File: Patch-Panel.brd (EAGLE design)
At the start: 84.9 x 142.3 mm, 66 parts, among them J1 APPPP45_PCB_VERT, J10 APPPP45_PCB_VERT, J11 APPPP45_PCB_VERT, J12 APPPP45_PCB_VERT, J13 APPPP45_PCB_VERT, J14 APPPP45_PCB_VERT, J15 APPPP45_PCB_VERT, J16 APPPP45_PCB_VERT, J17 APPPP45_PCB_VERT, J18 APPPP45_PCB_VERT, J19 APPPP45_PCB_VERT, J2 APPPP45_PCB_VERT, J20 APPPP45_PCB_VERT, J21 APPPP45_PCB_VERT, J22 APPPP45_PCB_VERT, J23 APPPP45_PCB_VERT, J24 APPPP45_PCB_VERT, J25 APPPP45_PCB_VERT, J26 APPPP45_PCB_VERT, J27 APPPP45_PCB_VERT, J28 APPPP45_PCB_VERT, J29 APPPP45_PCB_VERT, J3 APPPP45_PCB_VERT, J30 APPPP45_PCB_VERT, J31 APPPP45_PCB_VERT, J32 APPPP45_PCB_VERT, J33 APPPP45_PCB_VERT, J34 APPPP45_PCB_VERT, J35 APPPP45_PCB_VERT, J36 APPPP45_PCB_VERT, J37 APPPP45_PCB_VERT, J38 APPPP45_PCB_VERT, J39 APPPP45_PCB_VERT, J4 APPPP45_PCB_VERT, J40 APPPP45_PCB_VERT, J41 APPPP45_PCB_VERT, J42 APPPP45_PCB_VERT, J43 APPPP45_PCB_VERT, J44 APPPP45_PCB_VERT, J45 APPPP45_PCB_VERT, J46 APPPP45_PCB_VERT, J47 APPPP45_PCB_VERT, J48 APPPP45_PCB_VERT, J49 APPPP45_PCB_VERT, J5 APPPP45_PCB_VERT, J50 APPPP45_PCB_VERT, J51 APPPP45_PCB_VERT, J52 APPPP45_PCB_VERT, J53 APPPP45_PCB_VERT, J54 APPPP45_PCB_VERT, J55 APPPP45_PCB_VERT, J56 APPPP45_PCB_VERT, J57 APPPP45_PCB_VERT, J58 APPPP45_PCB_VERT, J6 APPPP45_PCB_VERT, J7 APPPP45_PCB_VERT, J8 APPPP45_PCB_VERT, J9 APPPP45_PCB_VERT

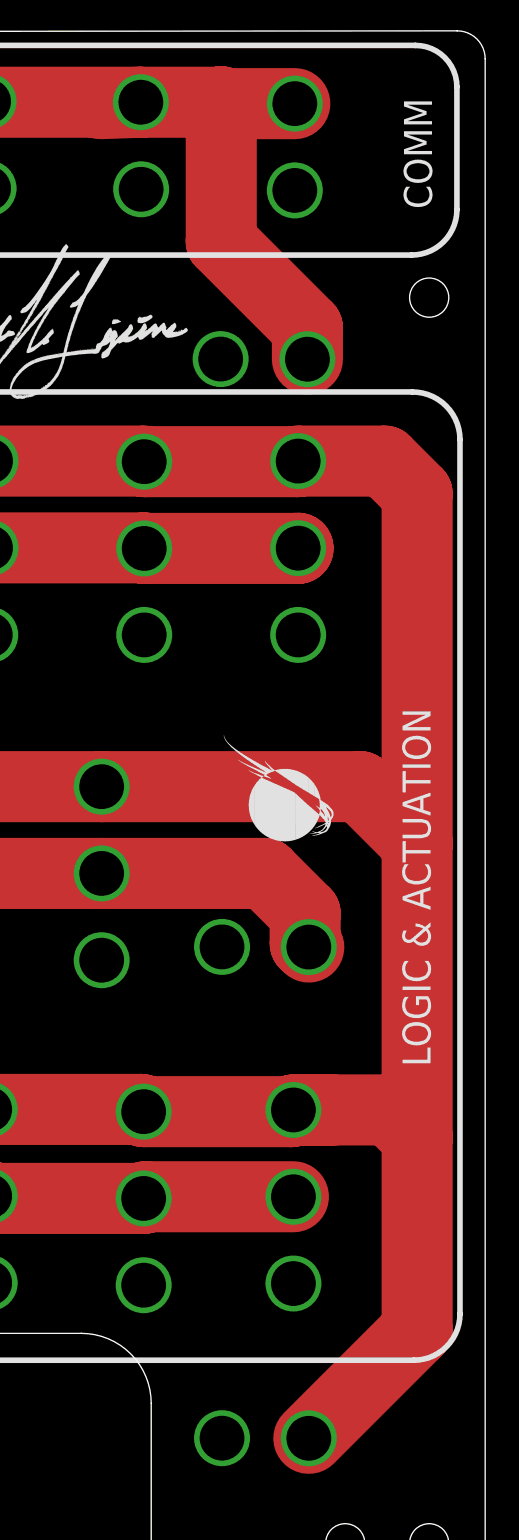
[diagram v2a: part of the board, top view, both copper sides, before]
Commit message: Adjusted bottom anderson positions
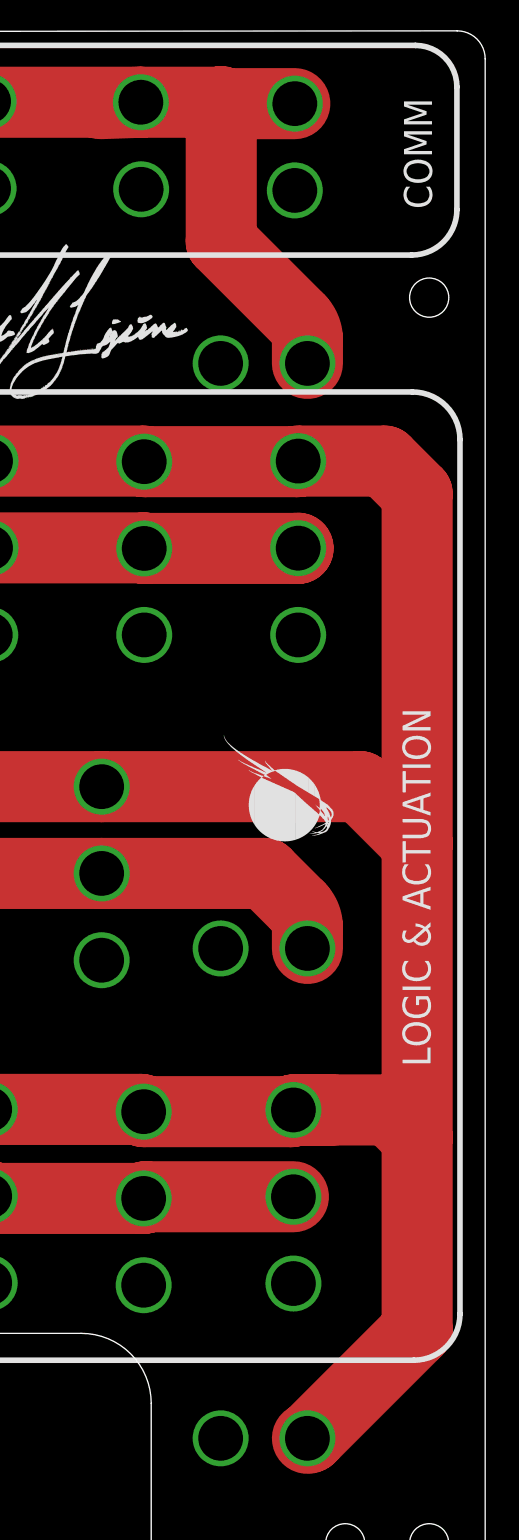
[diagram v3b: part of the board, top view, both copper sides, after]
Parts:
- moved J4 0.39 mm to (57.0, 115.3)
- moved J5 0.38 mm to (64.8, 115.3)
- moved J6 0.19 mm to (57.0, 62.2)
- moved J3 0.18 mm to (64.8, 62.2)
- moved J2 0.13 mm to (57.0, 17.8)
- moved J1 0.13 mm to (64.8, 17.8)
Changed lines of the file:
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@@
 <setting verticaltext="up"/>
 </settings>
-<grid distance="10" unitdist="mil" unit="mil" style="lines" multiple="1" display="yes" altdistance="5" altunitdist="mil" altunit="mil"/>
+<grid distance="1" unitdist="mil" unit="mil" style="lines" multiple="1" display="yes" altdistance="5" altunitdist="mil" altunit="mil"/>
 <layers>
 <layer number="1" name="Top" color="4" fill="1" visible="yes" active="yes"/>
@@
 <dimension x1="35.56" y1="24.13" x2="16.7894" y2="0" x3="-8.763" y3="12.065" textsize="1.778" layer="47" dtype="vertical" unit="mil"/>
 <wire x1="32.258" y1="120.142" x2="32.258" y2="112.014" width="0.254" layer="21"/>
+<dimension x1="82.3722" y1="0" x2="72.898" y2="9.906" x3="93.218" y3="4.953" textsize="1.4224" layer="21" dtype="vertical" unit="mil"/>
+<dimension x1="84.9122" y1="2.54" x2="72.7202" y2="10.9474" x3="78.8162" y3="-9.525" textsize="1.4224" layer="21" dtype="horizontal" unit="mil"/>
+<dimension x1="84.9122" y1="2.54" x2="72.7202" y2="10.414" x3="78.8162" y3="63.5254" textsize="1.4224" layer="21" dtype="horizontal" unit="mil"/>
+<dimension x1="82.3722" y1="0" x2="72.7202" y2="107.442" x3="112.903" y3="53.721" textsize="1.4224" layer="47" dtype="vertical" unit="mil"/>
+<dimension x1="82.3722" y1="0" x2="72.7202" y2="54.356" x3="98.1202" y3="27.178" textsize="1.4224" layer="47" dtype="vertical" unit="mil"/>
 </plain>
 <attributes>
@@
 </autorouter>
 <elements>
-<element name="J1" library="MRDT-Connectors" package="APP45_PCB_VERT" value="APPPP45_PCB_VERT" x="64.9732" y="17.78" rot="MR180">
-<attribute name="COLOR1" value="" x="64.9732" y="17.78" size="1.778" layer="28" rot="MR180" display="off"/>
+<element name="J1" library="MRDT-Connectors" package="APP45_PCB_VERT" value="APPPP45_PCB_VERT" x="64.8462" y="17.78" rot="MR180">
+<attribute name="COLOR1" value="" x="64.8462" y="17.78" size="1.778" layer="28" rot="MR180" display="off"/>
 </element>
 <element name="J10" library="MRDT-Connectors" package="APP45_PCB_VERT" value="APPPP45_PCB_VERT" x="50.7492" y="32.4358" rot="R270">
@@
 <attribute name="COLOR1" value="" x="34.2392" y="61.8744" size="1.778" layer="27" rot="R270" display="off"/>
 </element>
-<element name="J2" library="MRDT-Connectors" package="APP45_PCB_VERT" value="APPPP45_PCB_VERT" x="57.0992" y="17.7927" rot="MR180">
-<attribute name="COLOR1" value="" x="57.0992" y="17.7927" size="1.778" layer="28" rot="MR180" display="off"/>
+<element name="J2" library="MRDT-Connectors" package="APP45_PCB_VERT" value="APPPP45_PCB_VERT" x="56.9722" y="17.78" rot="MR180">
+<attribute name="COLOR1" value="" x="56.9722" y="17.78" size="1.778" layer="28" rot="MR180" display="off"/>
 </element>
 <element name="J20" library="MRDT-Connectors" package="APP45_PCB_VERT" value="APPPP45_PCB_VERT" x="34.2392" y="69.7484" rot="R270">
@@
 <attribute name="COLOR1" value="" x="46.9392" y="61.9252" size="1.778" layer="27" rot="R270" display="off"/>
 </element>
-<element name="J3" library="MRDT-Connectors" package="APP45_PCB_VERT" value="APPPP45_PCB_VERT" x="64.9732" y="62.357" rot="MR180">
-<attribute name="COLOR1" value="" x="64.9732" y="62.357" size="1.778" layer="28" rot="MR180" display="off"/>
+<element name="J3" library="MRDT-Connectors" package="APP45_PCB_VERT" value="APPPP45_PCB_VERT" x="64.8462" y="62.23" rot="MR180">
+<attribute name="COLOR1" value="" x="64.8462" y="62.23" size="1.778" layer="28" rot="MR180" display="off"/>
 </element>
 <element name="J30" library="MRDT-Connectors" package="APP45_PCB_VERT" value="APPPP45_PCB_VERT" x="64.4652" y="139.6492" rot="R270">
@@
 <attribute name="COLOR1" value="" x="22.7076" y="131.9784" size="1.778" layer="27" rot="R270" display="off"/>
 </element>
-<element name="J4" library="MRDT-Connectors" package="APP45_PCB_VERT" value="APPPP45_PCB_VERT" x="56.9722" y="115.7097" rot="MR180">
-<attribute name="COLOR1" value="" x="56.9722" y="115.7097" size="1.778" layer="28" rot="MR180" display="off"/>
-</element>
-<element name="J5" library="MRDT-Connectors" package="APP45_PCB_VERT" value="APPPP45_PCB_VERT" x="64.8462" y="115.697" rot="MR180">
-<attribute name="COLOR1" value="" x="64.8462" y="115.697" size="1.778" layer="28" rot="MR180" display="off"/>
-</element>
-<element name="J6" library="MRDT-Connectors" package="APP45_PCB_VERT" value="APPPP45_PCB_VERT" x="57.0992" y="62.3697" rot="MR180">
-<attribute name="COLOR1" value="" x="57.0992" y="62.3697" size="1.778" layer="28" rot="MR180" display="off"/>
+<element name="J4" library="MRDT-Connectors" package="APP45_PCB_VERT" value="APPPP45_PCB_VERT" x="56.9722" y="115.316" rot="MR180">
+<attribute name="COLOR1" value="" x="56.9722" y="115.316" size="1.778" layer="28" rot="MR180" display="off"/>
+</element>
+<element name="J5" library="MRDT-Connectors" package="APP45_PCB_VERT" value="APPPP45_PCB_VERT" x="64.8462" y="115.316" rot="MR180">
+<attribute name="COLOR1" value="" x="64.8462" y="115.316" size="1.778" layer="28" rot="MR180" display="off"/>
+</element>
+<element name="J6" library="MRDT-Connectors" package="APP45_PCB_VERT" value="APPPP45_PCB_VERT" x="56.9722" y="62.23" rot="MR180">
+<attribute name="COLOR1" value="" x="56.9722" y="62.23" size="1.778" layer="28" rot="MR180" display="off"/>
 </element>
 <element name="H3" library="MRDT-Hardware" package="#6_SCREW" value="MOUNTING_HOLE#6" x="9.9822" y="118.11"/>
@@
 <wire x1="24.7142" y1="73.6854" x2="24.6888" y2="73.7108" width="6.4516" layer="1"/>
 <wire x1="24.6888" y1="73.7108" x2="12.0142" y2="73.7108" width="6.4516" layer="1"/>
-<wire x1="68.9102" y1="14.605" x2="78.74" y2="24.4348" width="6.4516" layer="1"/>
 <wire x1="78.74" y1="41.91" x2="78.74" y2="24.4348" width="6.4516" layer="1"/>
 <wire x1="78.74" y1="41.91" x2="78.74" y2="68.58" width="6.4516" layer="1"/>
@@
 <wire x1="75.7936" y1="103.2764" x2="78.74" y2="100.33" width="6.4516" layer="1"/>
 <wire x1="78.74" y1="100.33" x2="78.74" y2="68.58" width="6.4516" layer="1"/>
+<wire x1="78.74" y1="24.4348" x2="69.000003125" y2="14.694803125" width="6.4516" layer="1"/>
+<wire x1="69.000003125" y1="14.694803125" x2="68.7832" y2="14.605" width="6.4516" layer="1" curve="-45"/>
 </signal>
 <signal name="LOG-12V">
@@
 <contactref element="J37" pad="P$1"/>
 <contactref element="J43" pad="P$1"/>
-<wire x1="68.9102" y1="59.182" x2="68.58" y2="59.5122" width="6.4516" layer="1"/>
-<wire x1="68.58" y1="59.5122" x2="68.58" y2="62.23" width="6.4516" layer="1"/>
-<wire x1="68.58" y1="62.23" x2="64.9478" y2="65.8622" width="6.4516" layer="1"/>
-<wire x1="64.9478" y1="65.8622" x2="50.1142" y2="65.8622" width="6.4516" layer="1"/>
+<wire x1="50.1142" y1="65.8622" x2="64.9478" y2="65.8622" width="6.4516" layer="1"/>
 <wire x1="50.1142" y1="65.8622" x2="37.465" y2="65.8622" width="6.4516" layer="1"/>
 <wire x1="37.465" y1="65.8622" x2="37.4142" y2="65.8114" width="6.4516" layer="1"/>
@@
 <wire x1="12.0142" y1="65.8368" x2="4.4704" y2="65.8368" width="6.4516" layer="1"/>
 <wire x1="4.4704" y1="65.8368" x2="4.2672" y2="66.04" width="6.4516" layer="1"/>
+<wire x1="64.9478" y1="65.8622" x2="68.03925" y2="62.77075" width="6.4516" layer="1"/>
+<wire x1="68.03925" y1="62.77075" x2="68.7832" y2="60.974696875" width="6.4516" layer="1" curve="-45.00007"/>
+<wire x1="68.7832" y1="60.974696875" x2="68.7832" y2="59.055" width="6.4516" layer="1"/>
 </signal>
 <signal name="COM-12V">
@@
 <wire x1="39.8526" y1="135.9154" x2="25.8826" y2="135.9154" width="6.4516" layer="1"/>
 <contactref element="J44" pad="P$1"/>
-<wire x1="68.7832" y1="112.522" x2="68.7832" y2="115.3668" width="6.4516" layer="1"/>
-<wire x1="68.7832" y1="115.3668" x2="60.96" y2="123.19" width="6.4516" layer="1"/>
-<wire x1="60.96" y1="123.19" x2="60.96" y2="135.89" width="6.4516" layer="1"/>
+<wire x1="60.96" y1="135.89" x2="60.96" y2="123.19" width="6.4516" layer="1"/>
 <wire x1="60.9092" y1="135.8392" x2="60.96" y2="135.89" width="6.4516" layer="1"/>
 <wire x1="60.9092" y1="135.8392" x2="53.6702" y2="135.8392" width="6.4516" layer="1"/>
@@
 <wire x1="25.8826" y1="135.9154" x2="12.1158" y2="135.9154" width="6.4516" layer="1"/>
 <wire x1="12.1158" y1="135.9154" x2="12.065" y2="135.8646" width="6.4516" layer="1"/>
+<wire x1="60.96" y1="123.19" x2="68.03925" y2="116.11075" width="6.4516" layer="1"/>
+<wire x1="68.03925" y1="116.11075" x2="68.7832" y2="114.314696875" width="6.4516" layer="1" curve="-45.00007"/>
+<wire x1="68.7832" y1="114.314696875" x2="68.7832" y2="112.141" width="6.4516" layer="1"/>
 </signal>
 </signals>
